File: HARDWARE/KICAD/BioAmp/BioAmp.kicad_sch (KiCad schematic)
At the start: 41 parts, among them U1 ADS1015IDGS, U2 LM324, U3 LM324

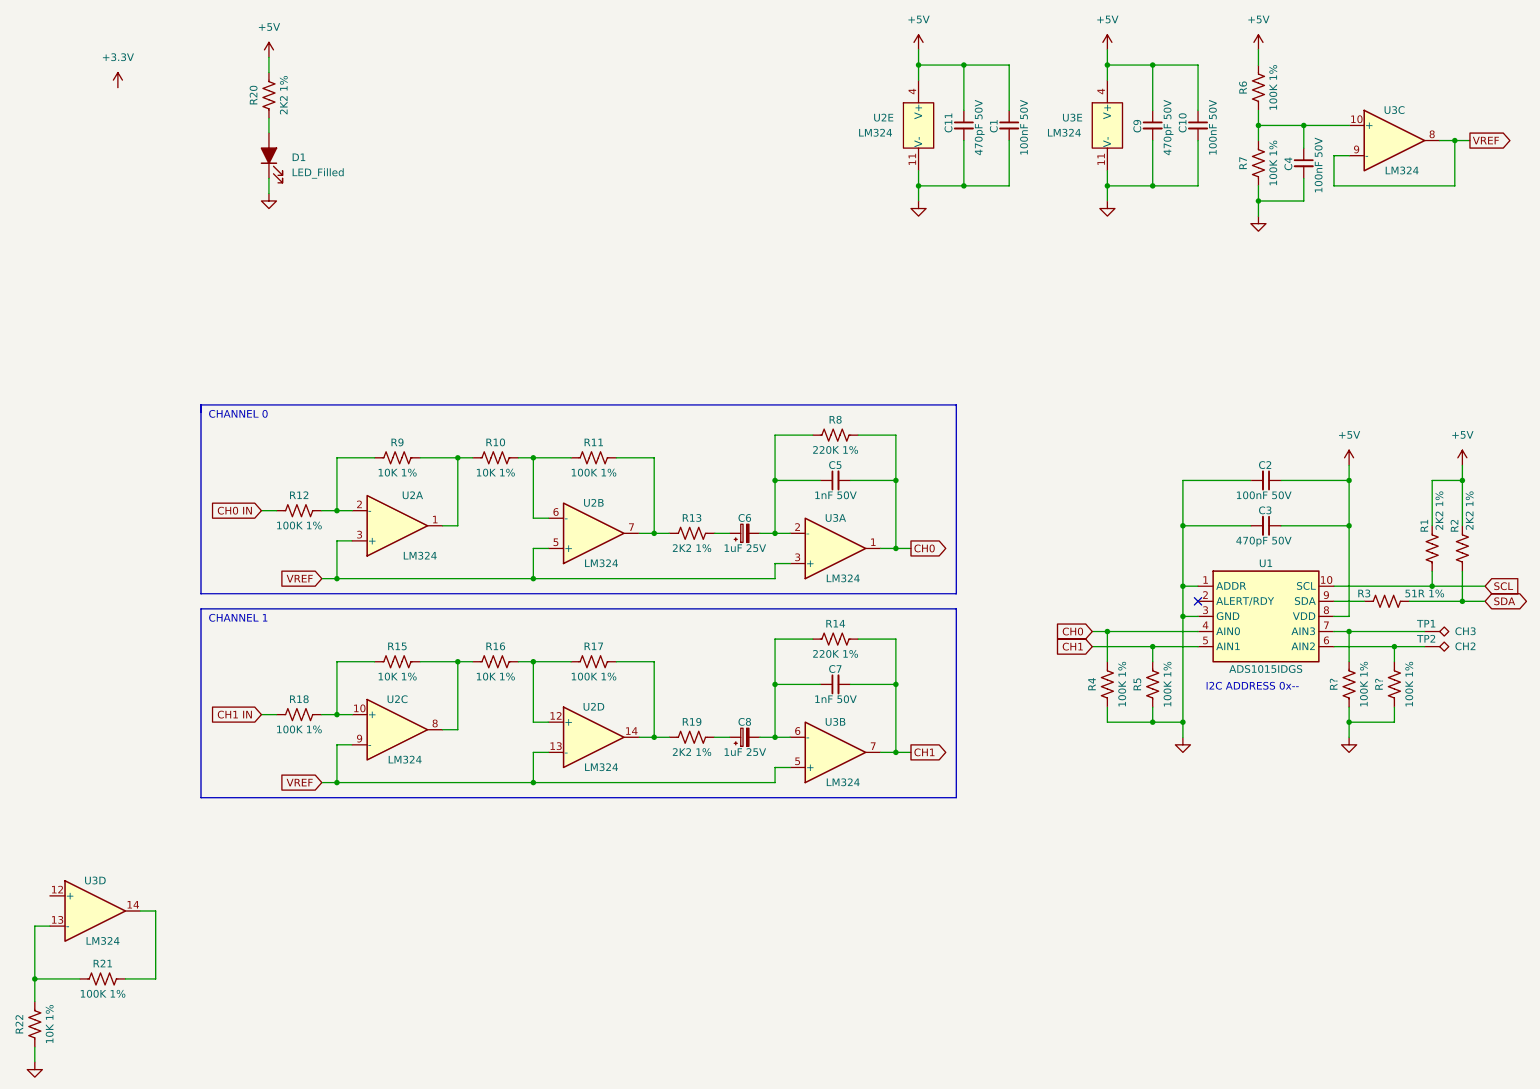
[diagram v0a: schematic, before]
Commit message: Esquemático com os circuitos separados por página e agrupados na página raiz.
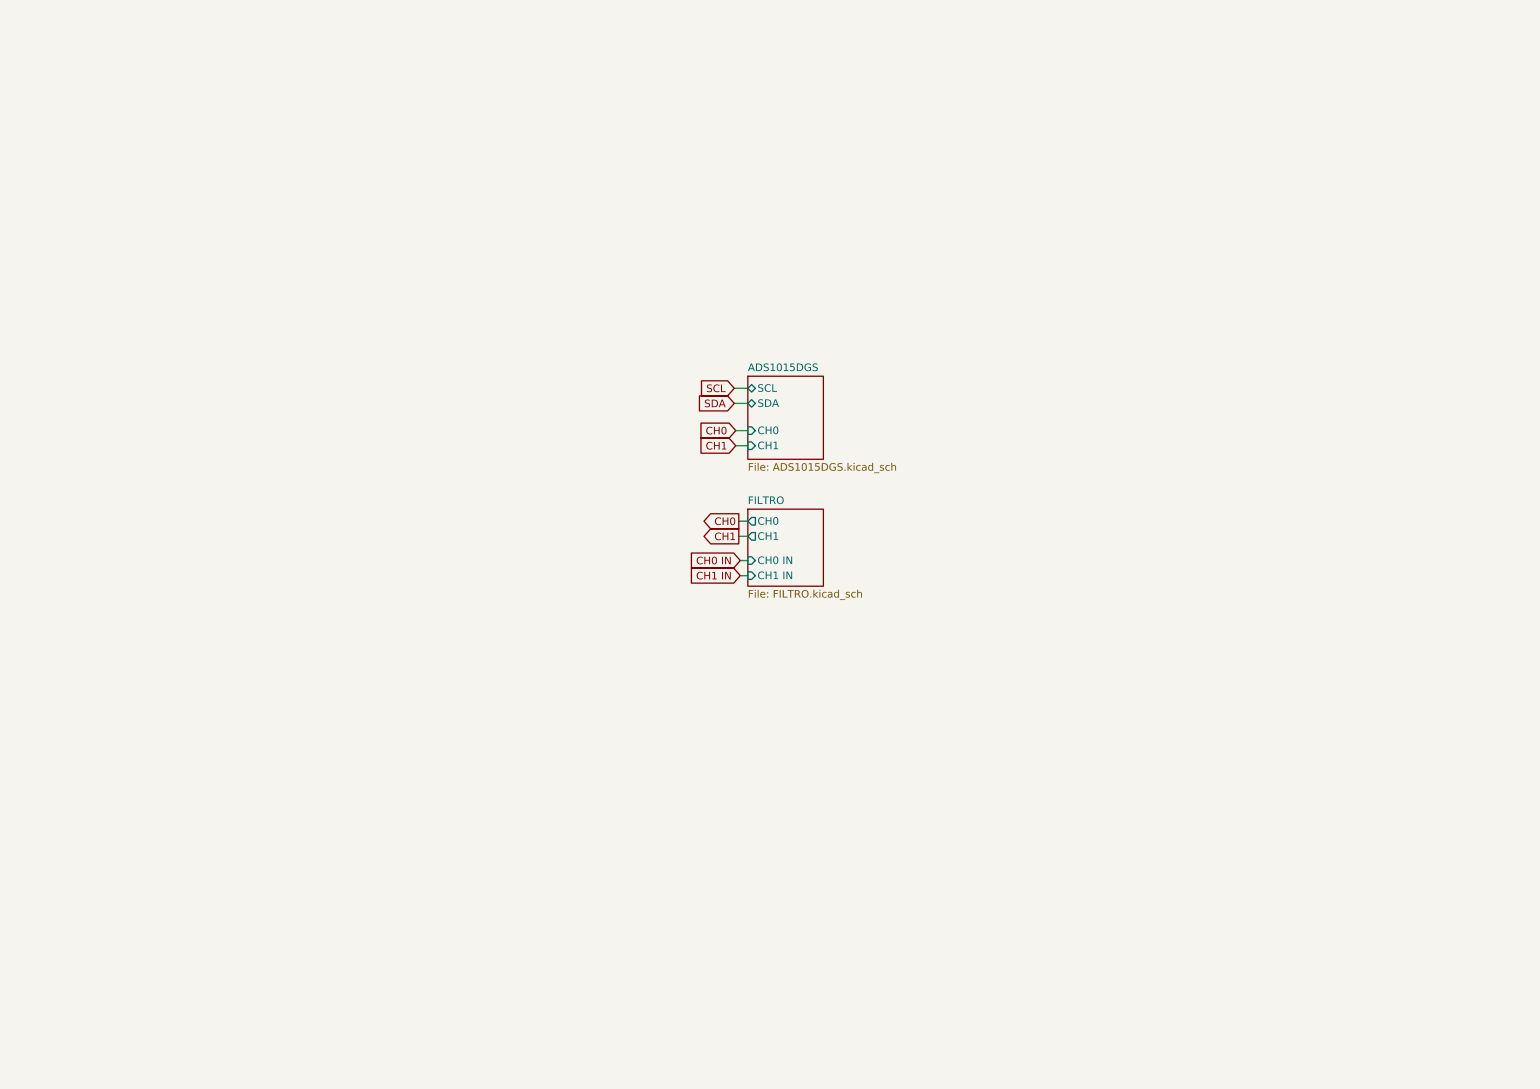
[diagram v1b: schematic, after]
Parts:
- removed C1, C10, C2, C4: 100nF 50V, symbol Device:C_Small
- removed C11, C3, C9: 470pF 50V, symbol Device:C_Small
- removed C5, C7: 1nF 50V, symbol Device:C_Small
- removed C6, C8: 1uF 25V, symbol Device:C_Polarized_Small
- removed D1: LED_Filled, symbol Device:LED_Filled
- removed R1, R13, R19, R2, R20: 2K2 1%, symbol Device:R_US
- removed R10, R15, R16, R22, R9: 10K 1%, symbol Device:R_US
- removed R11, R12, R17, R18, R21, R4, R5, R6, R7, R? (x2): 100K 1%, symbol Device:R_US
- removed R14, R8: 220K 1%, symbol Device:R_US
- removed R3: 51R 1%, symbol Device:R_US
- removed TP1: CH3, symbol Connector:TestPoint_Alt
- removed TP2: CH2, symbol Connector:TestPoint_Alt
- removed U1: ADS1015IDGS, Package_SO:TSSOP-10_3x3mm_P0.5mm, symbol Analog_ADC:ADS1015IDGS
- removed U2, U3: LM324, symbol Amplifier_Operational:LM324
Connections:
- no-connect marks 1 -> 0
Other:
- added sheet ADS1015DGS (ADS1015DGS.kicad_sch)
- added sheet FILTRO (FILTRO.kicad_sch)
- note removed: "CHANNEL 0"
- note removed: "CHANNEL 1"
- note removed: "I2C ADDRESS 0x--"

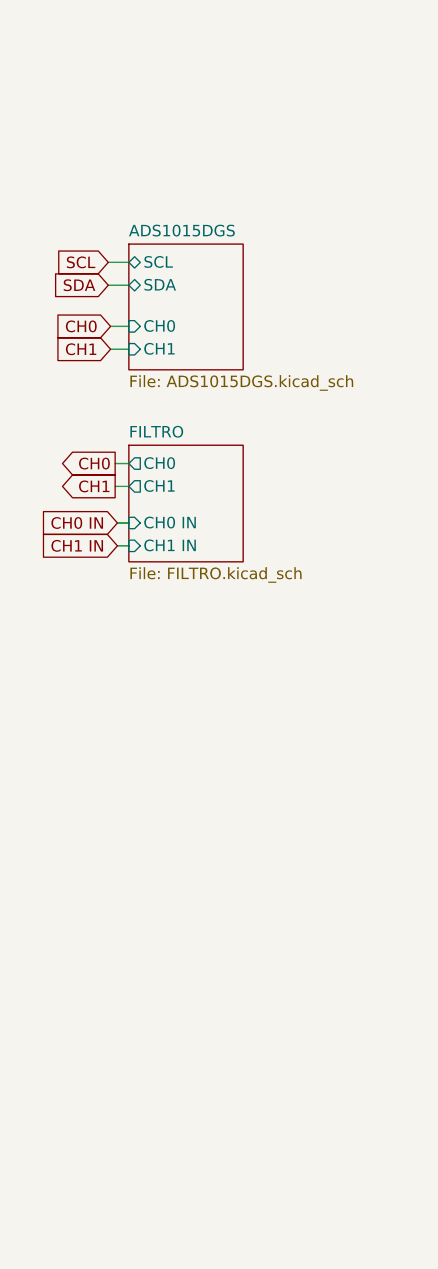
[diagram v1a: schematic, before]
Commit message: Adicionado o circuito de fonte ao esquemático, fonte para alimentações de até 20V e regulando para 5V e 3,3V.
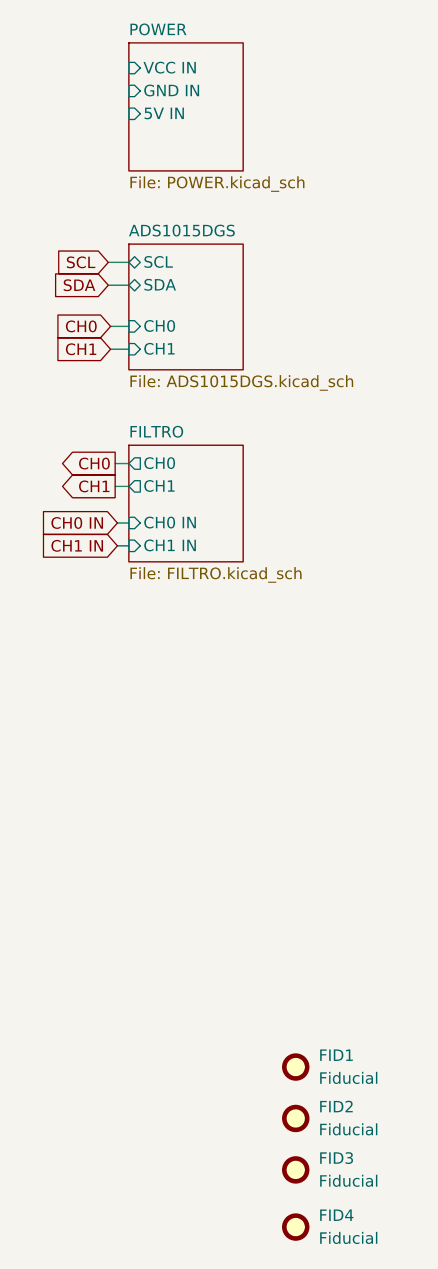
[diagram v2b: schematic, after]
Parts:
- added FID1, FID2, FID3, FID4: Fiducial, Fiducial:Fiducial_1.5mm_Mask3mm, symbol Mechanical:Fiducial
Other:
- added sheet POWER (POWER.kicad_sch)
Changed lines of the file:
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@@
+    )
+  )
+  (symbol (lib_id "Mechanical:Fiducial") (at 162.56 176.149 0) (unit 1)
+    (in_bom yes) (on_board yes) (dnp no) (fields_autoplaced)
+    (property "Reference" "FID2" (at 165.1 174.8789 0)
+      (effects (font (size 1.27 1.27)) (justify left))
+    )
+    (property "Value" "Fiducial" (at 165.1 177.4189 0)
+      (effects (font (size 1.27 1.27)) (justify left))
+    )
+    (property "Footprint" "Fiducial:Fiducial_1.5mm_Mask3mm" (at 162.56 176.149 0)
+      (effects (font (size 1.27 1.27)) hide)
+    )
+    (property "Datasheet" "~" (at 162.56 176.149 0)
+      (effects (font (size 1.27 1.27)) hide)
+    )
+    (instances
+      (project "BioAmp"
+        (path "/00c998d9-897a-42be-8000-a2ac18c402cc"
+          (reference "FID2") (unit 1)
+        )
+      )
+      (project "PCB_Central_Susp"
+        (path "/e63e39d7-6ac0-4ffd-8aa3-1841a4541b55"
+          (reference "FID2") (unit 1)
+        )
+      )
+    )
+  )
+  (symbol (lib_id "Mechanical:Fiducial") (at 162.56 170.434 0) (unit 1)
+    (in_bom yes) (on_board yes) (dnp no) (fields_autoplaced)
+    (property "Reference" "FID1" (at 165.1 169.1639 0)
+      (effects (font (size 1.27 1.27)) (justify left))
+    )
+    (property "Value" "Fiducial" (at 165.1 171.7039 0)
+      (effects (font (size 1.27 1.27)) (justify left))
+    )
+    (property "Footprint" "Fiducial:Fiducial_1.5mm_Mask3mm" (at 162.56 170.434 0)
+      (effects (font (size 1.27 1.27)) hide)
+    )
+    (property "Datasheet" "~" (at 162.56 170.434 0)
+      (effects (font (size 1.27 1.27)) hide)
+    )
+    (instances
+      (project "BioAmp"
+        (path "/00c998d9-897a-42be-8000-a2ac18c402cc"
+          (reference "FID1") (unit 1)
+        )
+      )
+      (project "PCB_Central_Susp"
+        (path "/e63e39d7-6ac0-4ffd-8aa3-1841a4541b55"
+          (reference "FID1") (unit 1)
+        )
+      )
+    )
+  )
+  (symbol (lib_id "Mechanical:Fiducial") (at 162.56 181.864 0) (unit 1)
+    (in_bom yes) (on_board yes) (dnp no) (fields_autoplaced)
+    (property "Reference" "FID3" (at 165.1 180.5939 0)
+      (effects (font (size 1.27 1.27)) (justify left))
+    )
+    (property "Value" "Fiducial" (at 165.1 183.1339 0)
+      (effects (font (size 1.27 1.27)) (justify left))
+    )
+    (property "Footprint" "Fiducial:Fiducial_1.5mm_Mask3mm" (at 162.56 181.864 0)
+      (effects (font (size 1.27 1.27)) hide)
+    )
+    (property "Datasheet" "~" (at 162.56 181.864 0)
+      (effects (font (size 1.27 1.27)) hide)
+    )
+    (instances
+      (project "BioAmp"
+        (path "/00c998d9-897a-42be-8000-a2ac18c402cc"
+          (reference "FID3") (unit 1)
+        )
+      )
+      (project "PCB_Central_Susp"
+        (path "/e63e39d7-6ac0-4ffd-8aa3-1841a4541b55"
+          (reference "FID3") (unit 1)
+        )
+      )
+    )
+  )
+  (symbol (lib_id "Mechanical:Fiducial") (at 162.56 188.214 0) (unit 1)
+    (in_bom yes) (on_board yes) (dnp no) (fields_autoplaced)
+    (property "Reference" "FID4" (at 165.1 186.9439 0)
+      (effects (font (size 1.27 1.27)) (justify left))
+    )
+    (property "Value" "Fiducial" (at 165.1 189.4839 0)
+      (effects (font (size 1.27 1.27)) (justify left))
+    )
+    (property "Footprint" "Fiducial:Fiducial_1.5mm_Mask3mm" (at 162.56 188.214 0)
+      (effects (font (size 1.27 1.27)) hide)
+    )
+    (property "Datasheet" "~" (at 162.56 188.214 0)
+      (effects (font (size 1.27 1.27)) hide)
+    )
+    (instances
+      (project "BioAmp"
+        (path "/00c998d9-897a-42be-8000-a2ac18c402cc"
+          (reference "FID4") (unit 1)
+        )
+      )
+      (project "PCB_Central_Susp"
+        (path "/e63e39d7-6ac0-4ffd-8aa3-1841a4541b55"
+          (reference "FID4") (unit 1)
+        )
+      )
+    )
+  )
+  (sheet (at 144.018 56.642) (size 12.7 14.224) (fields_autoplaced)
+    (stroke (width 0.1524) (type solid))
+    (fill (color 0 0 0 0.0000))
+    (property "Sheetname" "POWER" (at 144.018 55.9304 0)
+      (effects (font (size 1.27 1.27)) (justify left bottom))
+    )
+    (property "Sheetfile" "POWER.kicad_sch" (at 144.018 71.4506 0)
+      (effects (font (size 1.27 1.27)) (justify left top))
+    )
+    (pin "VCC IN" input (at 144.018 59.436 180)
+      (effects (font (size 1.27 1.27)) (justify left))
+    )
+    (pin "GND IN" input (at 144.018 61.976 180)
+      (effects (font (size 1.27 1.27)) (justify left))
+    )
+    (pin "5V IN" input (at 144.018 64.516 180)
+      (effects (font (size 1.27 1.27)) (justify left))
+    )
+    (instances
+      (project "BioAmp"
+        (path "/00c998d9-897a-42be-8000-a2ac18c402cc" (page "4"))
+      )
     )
   )

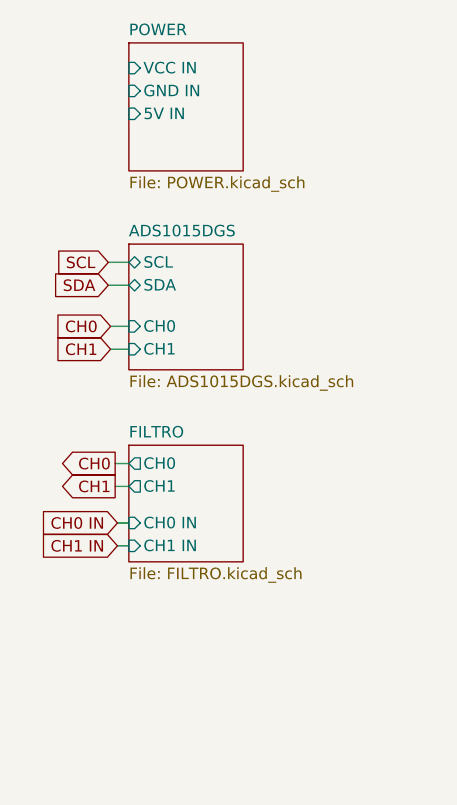
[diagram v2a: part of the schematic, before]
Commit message: Corrigido circuito AFE (Analog Front End); adição dos ports necessários na folha principal; transferência do LED de indicação de energia para folha de fontes; adição da sugestão para novo ADC.
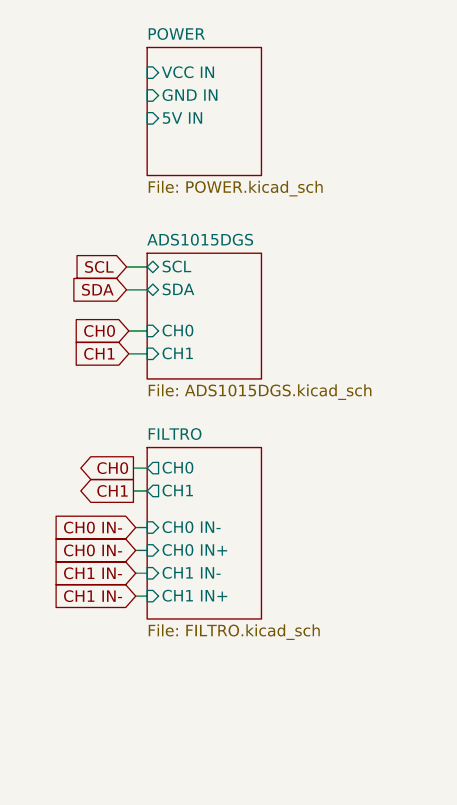
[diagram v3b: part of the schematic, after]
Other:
- sheet FILTRO ports: added CH0 IN+, CH0 IN-, CH1 IN+, CH1 IN-; removed CH0 IN, CH1 IN
